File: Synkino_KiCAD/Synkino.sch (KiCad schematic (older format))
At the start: 65 parts

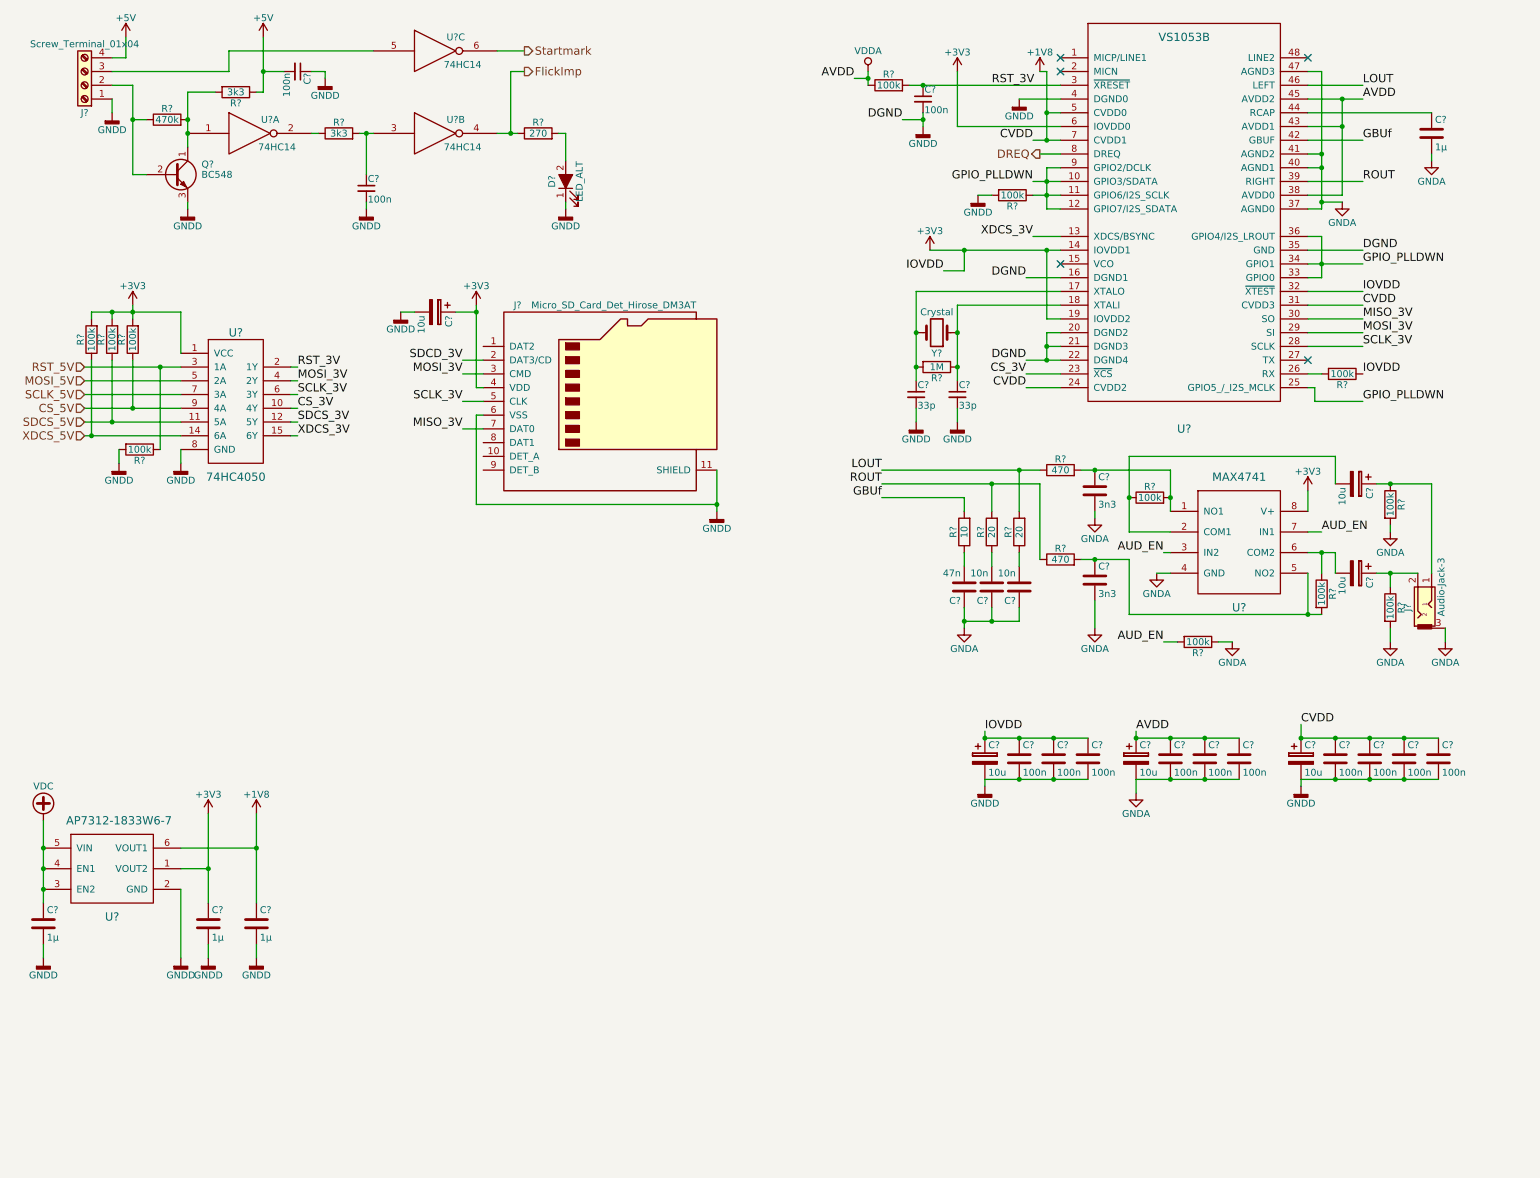
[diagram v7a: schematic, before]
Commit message: Adding 5V
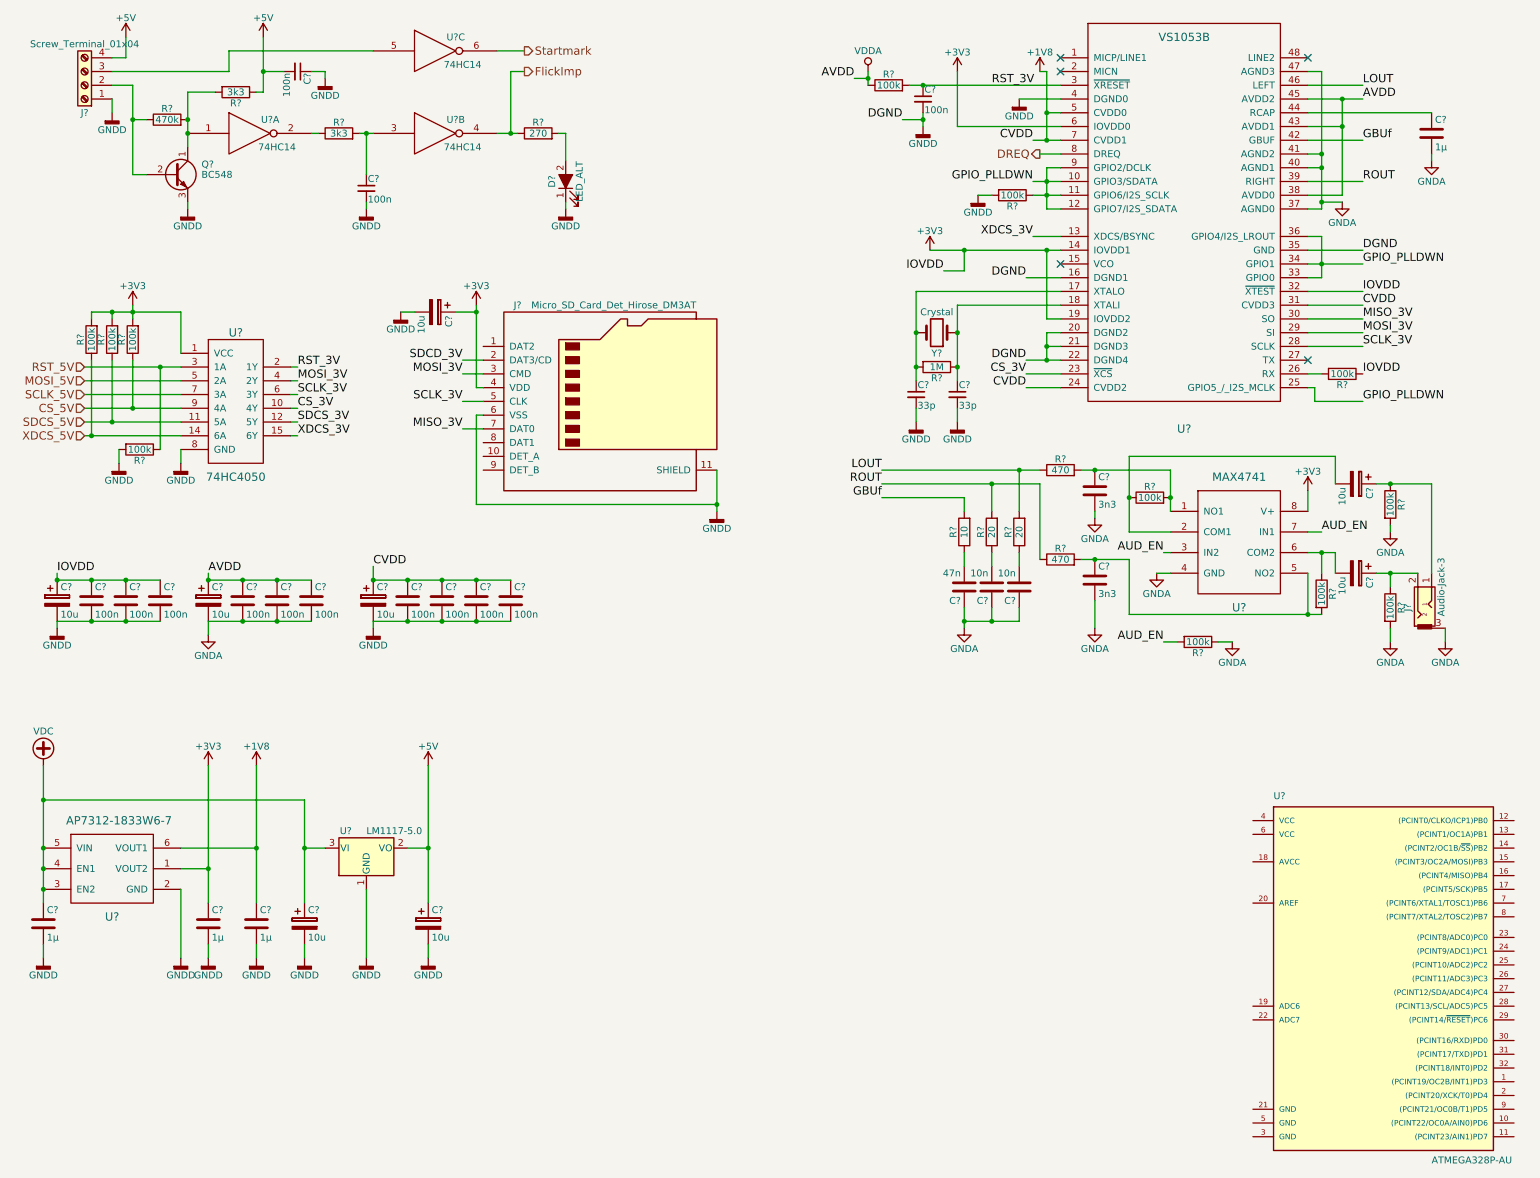
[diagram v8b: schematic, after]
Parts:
- added C? (x2): 10u, symbol CP
- added U?: ATMEGA328P-AU, Housings_QFP:TQFP-32_7x7mm_Pitch0.8mm, symbol ATMEGA328P-AU
- added U?: LM1117-5.0, symbol LM1117-5.0
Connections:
- net +5V: now also C?.1, U?.2 (VO)
- net GNDD: now also C?.2, C?.2, U?.1 (GND)
- net VDC: now also C?.1, U?.3 (VI)
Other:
- moved on the sheet: C?
